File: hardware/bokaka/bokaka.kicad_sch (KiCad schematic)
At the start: 0 parts

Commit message: Adding power and connector
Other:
- added sheet Connectors (connectors.kicad_sch)
- added sheet Microcontroller (microcontroller.kicad_sch)
- added sheet Power Supply (power.kicad_sch)
- company: (none) -> DIVA Engineering
- title: (none) -> BOKAKA
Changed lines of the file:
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@@
 	(generator_version "9.0")
 	(paper "A4")
+	(title_block
+		(title "BOKAKA")
+		(date "2025-12-09")
+		(rev "v1.0")
+		(company "DIVA Engineering")
+		(comment 3 "collectible at VOCALOID events.")
+		(comment 4 "Bokaka is an open-hardware, open-firmware credit-card–sized PCB distributed as a ")
+	)
+	(wire
+		(pts
+			(xy 92.71 80.01) (xy 88.9 80.01)
+		)
+		(stroke
+			(width 0)
+			(type default)
+		)
+	)
+	(wire
+		(pts
+			(xy 88.9 80.01) (xy 88.9 43.18)
+		)
+		(stroke
+			(width 0)
+			(type default)
+		)
+	)
+	(wire
+		(pts
+			(xy 90.17 77.47) (xy 92.71 77.47)
+		)
+		(stroke
+			(width 0)
+			(type default)
+		)
+	)
+	(wire
+		(pts
+			(xy 88.9 43.18) (xy 91.44 43.18)
+		)
+		(stroke
+			(width 0)
+			(type default)
+		)
+	)
+	(wire
+		(pts
+			(xy 91.44 45.72) (xy 90.17 45.72)
+		)
+		(stroke
+			(width 0)
+			(type default)
+		)
+	)
+	(wire
+		(pts
+			(xy 90.17 45.72) (xy 90.17 77.47)
+		)
+		(stroke
+			(width 0)
+			(type default)
+		)
+	)
+	(sheet
+		(at 92.71 74.93)
+		(size 39.37 22.86)
+		(exclude_from_sim no)
+		(in_bom yes)
+		(on_board yes)
+		(dnp no)
+		(fields_autoplaced yes)
+		(stroke
+			(width 0.1524)
+			(type solid)
+		)
+		(fill
+			(color 0 0 0 0.0000)
+		)
+		(property "Sheetname" "Microcontroller"
+			(at 92.71 74.2184 0)
+			(effects
+				(font
+					(size 1.27 1.27)
+				)
+				(justify left bottom)
+			)
+		)
+		(property "Sheetfile" "microcontroller.kicad_sch"
+			(at 92.71 98.3746 0)
+			(effects
+				(font
+					(size 1.27 1.27)
+				)
+				(justify left top)
+			)
+		)
+		(pin "USB_D+" input
+			(at 92.71 80.01 180)
+			(effects
+				(font
+					(size 1.27 1.27)
+				)
+				(justify left)
+			)
+		)
+		(pin "USB_D-" input
+			(at 92.71 77.47 180)
+			(effects
+				(font
+					(size 1.27 1.27)
+				)
+				(justify left)
+			)
+		)
+		(instances
+			(project "bokaka"
+				(path "/d8e340c0-2cae-427d-93e9-6fca5a11389e"
+					(page "4")
+				)
+			)
+		)
+	)
+	(sheet
+		(at 35.56 40.64)
+		(size 36.83 16.51)
+		(exclude_from_sim no)
+		(in_bom yes)
+		(on_board yes)
+		(dnp no)
+		(fields_autoplaced yes)
+		(stroke
+			(width 0.1524)
+			(type solid)
+		)
+		(fill
+			(color 0 0 0 0.0000)
+		)
+		(property "Sheetname" "Power Supply"
+			(at 35.56 39.9284 0)
+			(effects
+				(font
+					(size 1.27 1.27)
+				)
+				(justify left bottom)
+			)
+		)
+		(property "Sheetfile" "power.kicad_sch"
+			(at 35.56 57.7346 0)
+			(effects
+				(font
+					(size 1.27 1.27)
+				)
+				(justify left top)
+			)
+		)
+		(instances
+			(project "bokaka"
+				(path "/d8e340c0-2cae-427d-93e9-6fca5a11389e"
+					(page "2")
+				)
+			)
+		)
+	)
+	(sheet
+		(at 91.44 39.37)
+		(size 39.37 17.78)
+		(exclude_from_sim no)
+		(in_bom yes)
+		(on_board yes)
+		(dnp no)
+		(fields_autoplaced yes)
+		(stroke
+			(width 0.1524)
+			(type solid)
+		)
+		(fill
+			(color 0 0 0 0.0000)
+		)
+		(property "Sheetname" "Connectors"
+			(at 91.44 38.6584 0)
+			(effects
+				(font
+					(size 1.27 1.27)
+				)
+				(justify left bottom)
+			)
+		)
+		(property "Sheetfile" "connectors.kicad_sch"
+			(at 91.44 57.7346 0)
+			(effects
+				(font
+					(size 1.27 1.27)
+				)
+				(justify left top)
+			)
+		)
+		(pin "USB_D+" input
+			(at 91.44 43.18 180)
+			(effects
+				(font
+					(size 1.27 1.27)
+				)
+				(justify left)
+			)
+		)
+		(pin "USB_D-" input
+			(at 91.44 45.72 180)
+			(effects
+				(font
+					(size 1.27 1.27)
+				)
+				(justify left)
+			)
+		)
+		(instances
+			(project "bokaka"
+				(path "/d8e340c0-2cae-427d-93e9-6fca5a11389e"
+					(page "3")
+				)
+			)
+		)
+	)
 	(sheet_instances
 		(path "/"

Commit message: Adding rest of design and pdf
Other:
- added sheet Peripherals (peripherals.kicad_sch)
- sheet Connectors ports: added I2C_SCL, I2C_SDA, SWD_SWCLK, SWD_SWDIO, TAP_DATA, TAP_DETECT, UART_RX, UART_TX, ~{RESET}; removed none
- sheet Microcontroller ports: added BUZZ_PWM, I2C_SCL, I2C_SDA, LED_STATUS, SWD_SWCLK, SWD_SWDIO, TAP_DATA, TAP_DETECT, UART_RX, UART_TX, USR_BTN0, USR_BTN1, ~{BOOT_SEL}, ~{RESET}; removed none

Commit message: Finalize design before pcb
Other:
- sheet Microcontroller ports: added LED_DEBUG, LED_EN, LED_USER, TAP_IO, TAP_WAKE, USB_DETECT; removed LED_STATUS, TAP_DATA, TAP_DETECT
- sheet Peripherals ports: added LED_DEBUG, LED_EN, LED_I2C_SCL, LED_I2C_SDA; removed none
- sheet Power Supply ports: added USB_DETECT; removed none
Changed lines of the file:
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@@
 		(color 0 0 0 0)
 	)
+	(junction
+		(at 138.43 80.01)
+		(diameter 0)
+		(color 0 0 0 0)
+	)
+	(junction
+		(at 137.16 77.47)
+		(diameter 0)
+		(color 0 0 0 0)
+	)
+	(junction
+		(at 147.32 97.79)
+		(diameter 0)
+		(color 0 0 0 0)
+	)
 	(wire
 		(pts
@@
 	(wire
 		(pts
-			(xy 132.08 97.79) (xy 149.86 97.79)
+			(xy 147.32 97.79) (xy 149.86 97.79)
 		)
 		(stroke
@@
 	(wire
 		(pts
+			(xy 72.39 74.93) (xy 81.28 74.93)
+		)
+		(stroke
+			(width 0)
+			(type default)
+		)
+	)
+	(wire
+		(pts
+			(xy 132.08 92.71) (xy 149.86 92.71)
+		)
+		(stroke
+			(width 0)
+			(type default)
+		)
+	)
+	(wire
+		(pts
 			(xy 86.36 49.53) (xy 91.44 49.53)
 		)
@@
 	(wire
 		(pts
-			(xy 147.32 55.88) (xy 147.32 100.33)
-		)
-		(stroke
-			(width 0)
-			(type default)
-		)
-	)
-	(wire
-		(pts
 			(xy 139.7 82.55) (xy 132.08 82.55)
 		)
@@
 	(wire
 		(pts
-			(xy 138.43 80.01) (xy 132.08 80.01)
-		)
-		(stroke
-			(width 0)
-			(type default)
-		)
-	)
-	(wire
-		(pts
 			(xy 132.08 100.33) (xy 147.32 100.33)
 		)
@@
 	(wire
 		(pts
-			(xy 132.08 92.71) (xy 149.86 92.71)
-		)
-		(stroke
-			(width 0)
-			(type default)
-		)
-	)
-	(wire
-		(pts
 			(xy 92.71 90.17) (xy 85.09 90.17)
 		)
@@
 	(wire
 		(pts
+			(xy 81.28 74.93) (xy 81.28 101.6)
+		)
+		(stroke
+			(width 0)
+			(type default)
+		)
+	)
+	(wire
+		(pts
+			(xy 132.08 105.41) (xy 149.86 105.41)
+		)
+		(stroke
+			(width 0)
+			(type default)
+		)
+	)
+	(wire
+		(pts
+			(xy 132.08 77.47) (xy 137.16 77.47)
+		)
+		(stroke
+			(width 0)
+			(type default)
+		)
+	)
+	(wire
+		(pts
 			(xy 88.9 82.55) (xy 88.9 54.61)
 		)
@@
 	(wire
 		(pts
-			(xy 132.08 77.47) (xy 137.16 77.47)
-		)
-		(stroke
-			(width 0)
-			(type default)
-		)
-	)
-	(wire
-		(pts
 			(xy 130.81 41.91) (xy 140.97 41.91)
 		)
@@
 	(wire
 		(pts
-			(xy 132.08 105.41) (xy 149.86 105.41)
+			(xy 132.08 80.01) (xy 138.43 80.01)
+		)
+		(stroke
+			(width 0)
+			(type default)
+		)
+	)
+	(wire
+		(pts
+			(xy 138.43 80.01) (xy 149.86 80.01)
+		)
+		(stroke
+			(width 0)
+			(type default)
+		)
+	)
+	(wire
+		(pts
+			(xy 147.32 97.79) (xy 147.32 100.33)
 		)
 		(stroke
@@
 	(wire
 		(pts
+			(xy 132.08 90.17) (xy 149.86 90.17)
+		)
+		(stroke
+			(width 0)
+			(type default)
+		)
+	)
+	(wire
+		(pts
 			(xy 137.16 52.07) (xy 130.81 52.07)
 		)
@@
 	(wire
 		(pts
+			(xy 132.08 87.63) (xy 149.86 87.63)
+		)
+		(stroke
+			(width 0)
+			(type default)
+		)
+	)
+	(wire
+		(pts
+			(xy 147.32 55.88) (xy 147.32 97.79)
+		)
+		(stroke
+			(width 0)
+			(type default)
+		)
+	)
+	(wire
+		(pts
+			(xy 132.08 102.87) (xy 149.86 102.87)
+		)
+		(stroke
+			(width 0)
+			(type default)
+		)
+	)
+	(wire
+		(pts
 			(xy 92.71 85.09) (xy 87.63 85.09)
 		)
@@
 	(wire
 		(pts
+			(xy 137.16 77.47) (xy 149.86 77.47)
+		)
+		(stroke
+			(width 0)
+			(type default)
+		)
+	)
+	(wire
+		(pts
 			(xy 87.63 52.07) (xy 91.44 52.07)
 		)
@@
 	(wire
 		(pts
-			(xy 132.08 90.17) (xy 149.86 90.17)
-		)
-		(stroke
-			(width 0)
-			(type default)
-		)
-	)
-	(wire
-		(pts
 			(xy 91.44 44.45) (xy 83.82 44.45)
 		)
@@
 	(wire
 		(pts
+			(xy 147.32 97.79) (xy 132.08 97.79)
+		)
+		(stroke
+			(width 0)
+			(type default)
+		)
+	)
+	(wire
+		(pts
+			(xy 132.08 95.25) (xy 149.86 95.25)
+		)
+		(stroke
+			(width 0)
+			(type default)
+		)
+	)
+	(wire
+		(pts
 			(xy 138.43 49.53) (xy 138.43 80.01)
 		)
@@
 	(wire
 		(pts
-			(xy 132.08 95.25) (xy 149.86 95.25)
-		)
-		(stroke
-			(width 0)
-			(type default)
-		)
-	)
-	(wire
-		(pts
 			(xy 85.09 46.99) (xy 91.44 46.99)
+		)
+		(stroke
+			(width 0)
+			(type default)
+		)
+	)
+	(wire
+		(pts
+			(xy 81.28 101.6) (xy 92.71 101.6)
 		)
 		(stroke
@@
 			)
 		)
-		(pin "LED_STATUS" input
-			(at 132.08 90.17 0)
-			(effects
-				(font
-					(size 1.27 1.27)
-				)
-				(justify right)
-			)
-		)
 		(pin "SWD_SWCLK" input
 			(at 132.08 85.09 0)
@@
 			)
 		)
-		(pin "TAP_DATA" input
+		(pin "TAP_IO" input
 			(at 92.71 90.17 180)
-			(effects
-				(font
-					(size 1.27 1.27)
-				)
-				(justify left)
-			)
-		)
-		(pin "TAP_DETECT" input
-			(at 92.71 87.63 180)
 			(effects
 				(font
@@
 				)
 				(justify right)
+			)
+		)
+		(pin "LED_DEBUG" input
+			(at 132.08 87.63 0)
+			(effects
+				(font
+					(size 1.27 1.27)
+				)
+				(justify right)
+			)
+		)
+		(pin "LED_USER" input
+			(at 132.08 90.17 0)
+			(effects
+				(font
+					(size 1.27 1.27)
+				)
+				(justify right)
+			)
+		)
+		(pin "TAP_WAKE" input
+			(at 92.71 87.63 180)
+			(effects
+				(font
+					(size 1.27 1.27)
+				)
+				(justify left)
+			)
+		)
+		(pin "LED_EN" input
+			(at 132.08 102.87 0)
+			(effects
+				(font
+					(size 1.27 1.27)
+				)
+				(justify right)
+			)
+		)
+		(pin "USB_DETECT" input
+			(at 92.71 101.6 180)
+			(effects
+				(font
+					(size 1.27 1.27)
+				)
+				(justify left)
 			)
 		)
@@
 			)
 		)
+		(pin "USB_DETECT" input
+			(at 72.39 74.93 0)
+			(effects
+				(font
+					(size 1.27 1.27)
+				)
+				(justify right)
+			)
+		)
 		(instances
 			(project "bokaka"
@@
 	)
 	(sheet
-		(at 149.86 83.82)
-		(size 31.75 24.13)
+		(at 149.86 74.93)
+		(size 31.75 33.02)
 		(exclude_from_sim no)
 		(in_bom yes)
@@
 		)
 		(property "Sheetname" "Peripherals"
-			(at 149.86 83.1084 0)
+			(at 149.86 74.2184 0)
 			(effects
 				(font
@@
 			(effects
 				(font
+					(size 1.27 1.27)
+				)
+				(justify left)
+			)
+		)
+		(pin "LED_DEBUG" input
+			(at 149.86 87.63 180)
+			(effects
+				(font
+					(size 1.27 1.27)
+				)
+				(justify left)
+			)
+		)
+		(pin "LED_I2C_SCL" input
+			(at 149.86 80.01 180)
+			(effects
+				(font
+					(size 1.27 1.27)
+				)
+				(justify left)
+			)
+		)
+		(pin "LED_I2C_SDA" input
+			(at 149.86 77.47 180)
+			(effects
+				(font
+					(size 1.27 1.27)
+				)
+				(justify left)
+			)
+		)
+		(pin "LED_EN" input
+			(at 149.86 102.87 180)
+			(effects
+				(font

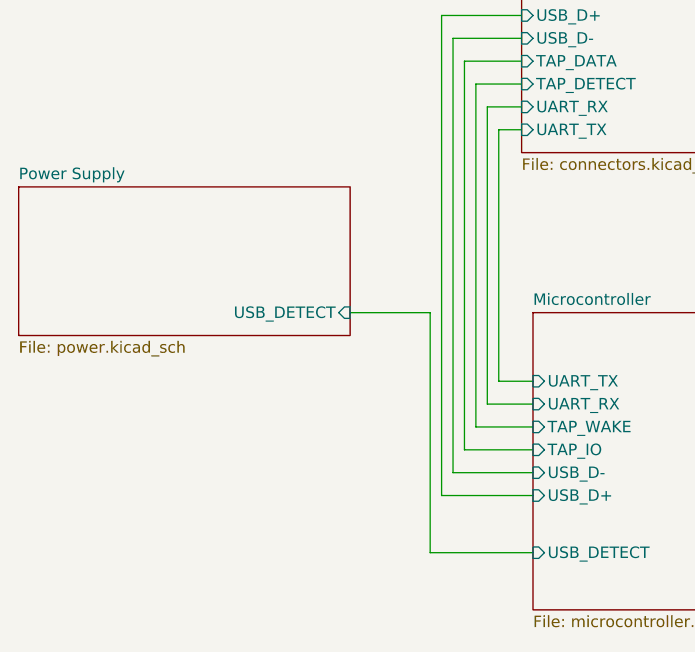
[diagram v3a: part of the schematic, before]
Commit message: footprint asignment
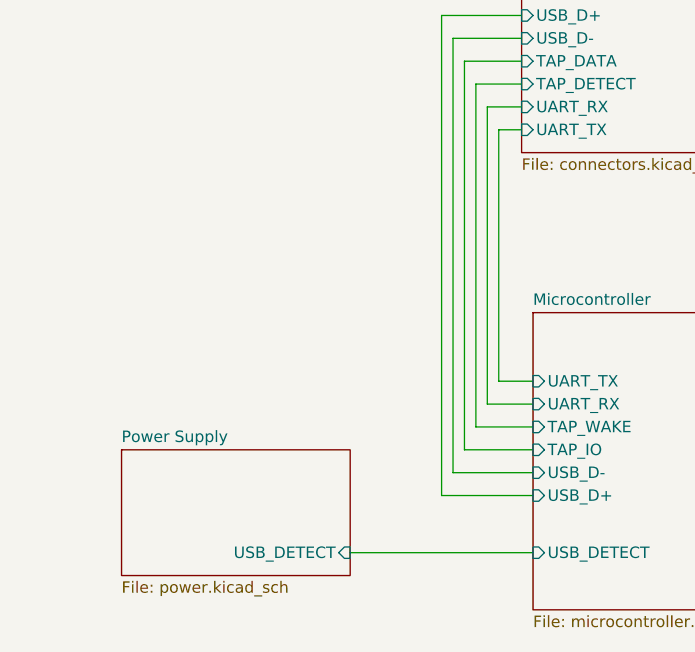
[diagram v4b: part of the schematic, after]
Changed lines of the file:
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@@
 	(wire
 		(pts
-			(xy 72.39 74.93) (xy 81.28 74.93)
+			(xy 72.39 101.6) (xy 92.71 101.6)
 		)
 		(stroke
@@
 	(wire
 		(pts
-			(xy 81.28 74.93) (xy 81.28 101.6)
-		)
-		(stroke
-			(width 0)
-			(type default)
-		)
-	)
-	(wire
-		(pts
 			(xy 132.08 105.41) (xy 149.86 105.41)
 		)
@@
 		(pts
 			(xy 85.09 46.99) (xy 91.44 46.99)
-		)
-		(stroke
-			(width 0)
-			(type default)
-		)
-	)
-	(wire
-		(pts
-			(xy 81.28 101.6) (xy 92.71 101.6)
 		)
 		(stroke
@@
 	)
 	(sheet
-		(at 35.56 60.96)
-		(size 36.83 16.51)
+		(at 46.99 90.17)
+		(size 25.4 13.97)
 		(exclude_from_sim no)
 		(in_bom yes)
@@
 		)
 		(property "Sheetname" "Power Supply"
-			(at 35.56 60.2484 0)
+			(at 46.99 89.4584 0)
 			(effects
 				(font
@@
 		)
 		(property "Sheetfile" "power.kicad_sch"
-			(at 35.56 78.0546 0)
+			(at 46.99 104.7246 0)
 			(effects
 				(font
@@
 		)
 		(pin "USB_DETECT" input
-			(at 72.39 74.93 0)
-			(effects
-				(font
+			(at 72.39 101.6 0)
+			(effects
+				(font

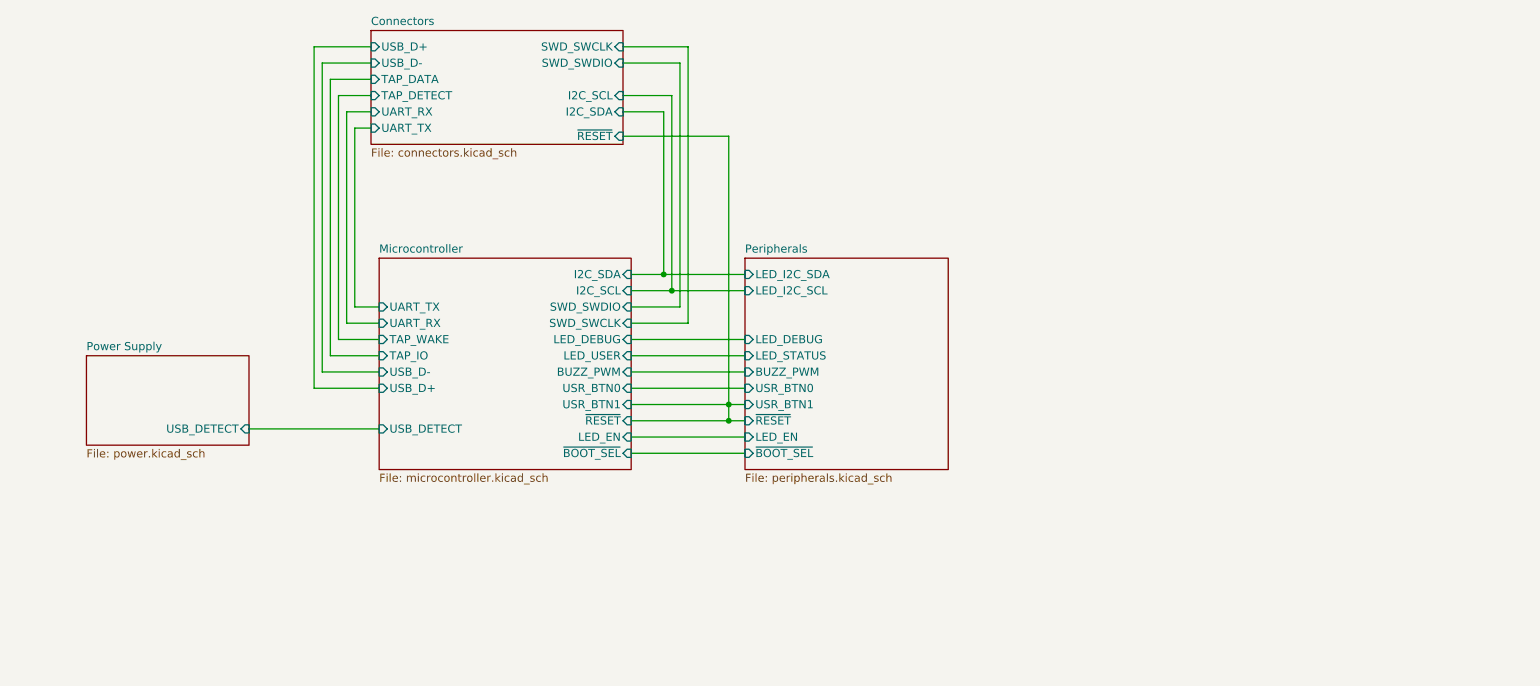
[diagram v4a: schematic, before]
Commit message: schematic update
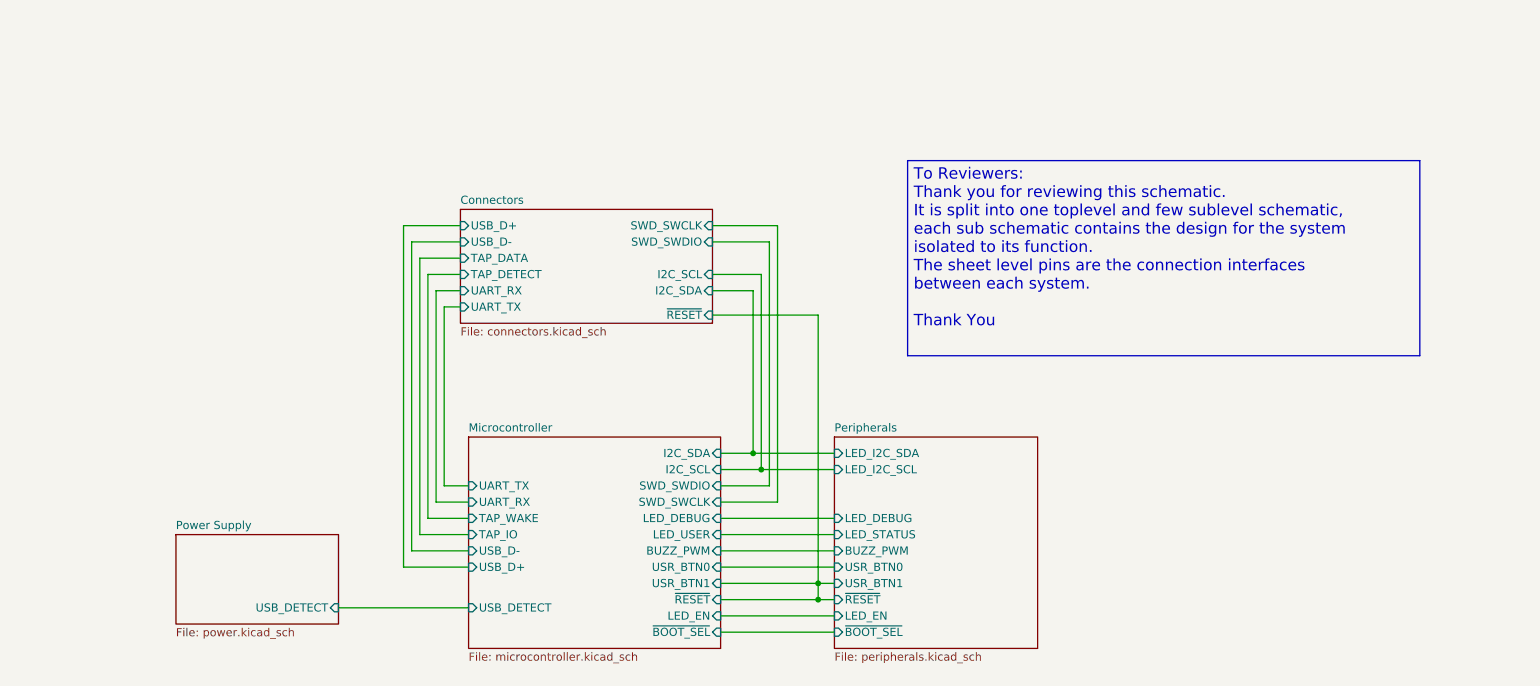
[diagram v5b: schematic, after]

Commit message: hardware update
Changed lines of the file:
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@@
 	)
 	(junction
-		(at 161.29 128.27)
+		(at 198.12 128.27)
 		(diameter 0)
 		(color 0 0 0 0)
@@
 		(color 0 0 0 0)
 	)
-	(junction
-		(at 161.29 125.73)
-		(diameter 0)
-		(color 0 0 0 0)
+	(wire
+		(pts
+			(xy 198.12 99.06) (xy 198.12 128.27)
+		)
+		(stroke
+			(width 0)
+			(type default)
+		)
 	)
 	(wire
@@
 	(wire
 		(pts
-			(xy 161.29 125.73) (xy 163.83 125.73)
-		)
-		(stroke
-			(width 0)
-			(type default)
-		)
-	)
-	(wire
-		(pts
 			(xy 106.68 123.19) (xy 96.52 123.19)
 		)
@@
 	(wire
 		(pts
+			(xy 146.05 133.35) (xy 161.29 133.35)
+		)
+		(stroke
+			(width 0)
+			(type default)
+		)
+	)
+	(wire
+		(pts
 			(xy 153.67 110.49) (xy 146.05 110.49)
 		)
@@
 	(wire
 		(pts
-			(xy 146.05 128.27) (xy 161.29 128.27)
-		)
-		(stroke
-			(width 0)
-			(type default)
-		)
-	)
-	(wire
-		(pts
 			(xy 99.06 118.11) (xy 99.06 74.93)
 		)
@@
 	(wire
 		(pts
+			(xy 161.29 83.82) (xy 161.29 99.06)
+		)
+		(stroke
+			(width 0)
+			(type default)
+		)
+	)
+	(wire
+		(pts
 			(xy 106.68 118.11) (xy 99.06 118.11)
 		)
@@
 	(wire
 		(pts
-			(xy 146.05 133.35) (xy 163.83 133.35)
+			(xy 146.05 130.81) (xy 163.83 130.81)
 		)
 		(stroke
@@
 	(wire
 		(pts
+			(xy 161.29 139.7) (xy 198.12 139.7)
+		)
+		(stroke
+			(width 0)
+			(type default)
+		)
+	)
+	(wire
+		(pts
 			(xy 146.05 107.95) (xy 152.4 107.95)
 		)
@@
 	(wire
 		(pts
+			(xy 198.12 128.27) (xy 195.58 128.27)
+		)
+		(stroke
+			(width 0)
+			(type default)
+		)
+	)
+	(wire
+		(pts
 			(xy 152.4 107.95) (xy 163.83 107.95)
 		)
@@
 	(wire
 		(pts
-			(xy 161.29 125.73) (xy 161.29 128.27)
-		)
-		(stroke
-			(width 0)
-			(type default)
-		)
-	)
-	(wire
-		(pts
 			(xy 96.52 69.85) (xy 105.41 69.85)
 		)
@@
 	(wire
 		(pts
-			(xy 161.29 83.82) (xy 161.29 125.73)
-		)
-		(stroke
-			(width 0)
-			(type default)
-		)
-	)
-	(wire
-		(pts
-			(xy 146.05 130.81) (xy 163.83 130.81)
+			(xy 161.29 133.35) (xy 161.29 139.7)
+		)
+		(stroke
+			(width 0)
+			(type default)
+		)
+	)
+	(wire
+		(pts
+			(xy 146.05 128.27) (xy 163.83 128.27)
 		)
 		(stroke
@@
 	(wire
 		(pts
-			(xy 161.29 128.27) (xy 163.83 128.27)
-		)
-		(stroke
-			(width 0)
-			(type default)
-		)
-	)
-	(wire
-		(pts
 			(xy 151.13 105.41) (xy 163.83 105.41)
 		)
@@
 	(wire
 		(pts
-			(xy 161.29 125.73) (xy 146.05 125.73)
+			(xy 146.05 125.73) (xy 163.83 125.73)
+		)
+		(stroke
+			(width 0)
+			(type default)
+		)
+	)
+	(wire
+		(pts
+			(xy 161.29 99.06) (xy 198.12 99.06)
 		)
 		(stroke
@@
 		(pts
 			(xy 152.4 77.47) (xy 152.4 107.95)
+		)
+		(stroke
+			(width 0)
+			(type default)
+		)
+	)
+	(wire
+		(pts
+			(xy 198.12 139.7) (xy 198.12 128.27)
 		)
 		(stroke
@@
 		)
 		(pin "~{RESET}" input
-			(at 146.05 128.27 0)
+			(at 146.05 133.35 0)
 			(effects
 				(font
@@
 		)
 		(pin "~{BOOT_SEL}" input
-			(at 146.05 133.35 0)
+			(at 146.05 130.81 0)
 			(effects
 				(font
@@
 		)
 		(pin "LED_EN" input
-			(at 146.05 130.81 0)
+			(at 146.05 128.27 0)
 			(effects
 				(font
@@
 		)
 		(pin "~{RESET}" input
-			(at 163.83 128.27 180)
-			(effects
-				(font
-					(size 1.27 1.27)
-				)
-				(justify left)
+			(at 195.58 128.27 0)
+			(effects
+				(font
+					(size 1.27 1.27)
+				)
+				(justify right)
 			)
 		)
@@
 		)
 		(pin "~{BOOT_SEL}" input
-			(at 163.83 133.35 180)
+			(at 163.83 130.81 180)
 			(effects
 				(font
@@
 		)
 		(pin "LED_EN" input
-			(at 163.83 130.81 180)
-			(effects
-				(font
+			(at 163.83 128.27 180)
+			(effects
+				(font

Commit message: Devkit Production Ready
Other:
- sheet Connectors ports: added none; removed I2C_SCL, I2C_SDA
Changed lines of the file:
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@@
 		(color 0 0 0 0)
 	)
-	(junction
-		(at 152.4 107.95)
-		(diameter 0)
-		(color 0 0 0 0)
-	)
-	(junction
-		(at 151.13 105.41)
-		(diameter 0)
-		(color 0 0 0 0)
-	)
 	(wire
 		(pts
@@
 	(wire
 		(pts
-			(xy 151.13 105.41) (xy 151.13 80.01)
-		)
-		(stroke
-			(width 0)
-			(type default)
-		)
-	)
-	(wire
-		(pts
 			(xy 146.05 133.35) (xy 161.29 133.35)
 		)
@@
 	(wire
 		(pts
-			(xy 146.05 105.41) (xy 151.13 105.41)
-		)
-		(stroke
-			(width 0)
-			(type default)
-		)
-	)
-	(wire
-		(pts
 			(xy 102.87 110.49) (xy 102.87 82.55)
 		)
@@
 	(wire
 		(pts
-			(xy 146.05 107.95) (xy 152.4 107.95)
-		)
-		(stroke
-			(width 0)
-			(type default)
-		)
-	)
-	(wire
-		(pts
 			(xy 198.12 128.27) (xy 195.58 128.27)
 		)
@@
 	(wire
 		(pts
-			(xy 152.4 107.95) (xy 163.83 107.95)
+			(xy 146.05 107.95) (xy 163.83 107.95)
 		)
 		(stroke
@@
 	(wire
 		(pts
-			(xy 151.13 80.01) (xy 144.78 80.01)
-		)
-		(stroke
-			(width 0)
-			(type default)
-		)
-	)
-	(wire
-		(pts
-			(xy 144.78 77.47) (xy 152.4 77.47)
-		)
-		(stroke
-			(width 0)
-			(type default)
-		)
-	)
-	(wire
-		(pts
 			(xy 101.6 113.03) (xy 101.6 80.01)
 		)
@@
 	(wire
 		(pts
-			(xy 151.13 105.41) (xy 163.83 105.41)
+			(xy 146.05 105.41) (xy 163.83 105.41)
 		)
 		(stroke
@@
 		(pts
 			(xy 146.05 123.19) (xy 163.83 123.19)
-		)
-		(stroke
-			(width 0)
-			(type default)
-		)
-	)
-	(wire
-		(pts
-			(xy 152.4 77.47) (xy 152.4 107.95)
 		)
 		(stroke
@@
 			(effects
 				(font
-					(size 1.27 1.27)
-				)
-				(justify right)
-			)
-		)
-		(pin "I2C_SCL" input
-			(at 144.78 77.47 0)
-			(effects
-				(font
-					(size 1.27 1.27)
-				)
-				(justify right)
-			)
-		)
-		(pin "I2C_SDA" input
-			(at 144.78 80.01 0)
-			(effects
-				(font
